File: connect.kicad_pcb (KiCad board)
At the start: 4 copper layers, 80 x 34.5 mm, 81 parts, among them J101 Cortex, J102 DX07S016JA3, J201 NE8FAH, J301 SJ2-25404B-SMT-TR, J401 SJ2-25404B-SMT-TR, SW101 SKSG, SW102 SKSG, SW103 SKSG, SW104 SKSG, SW105 SKSG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

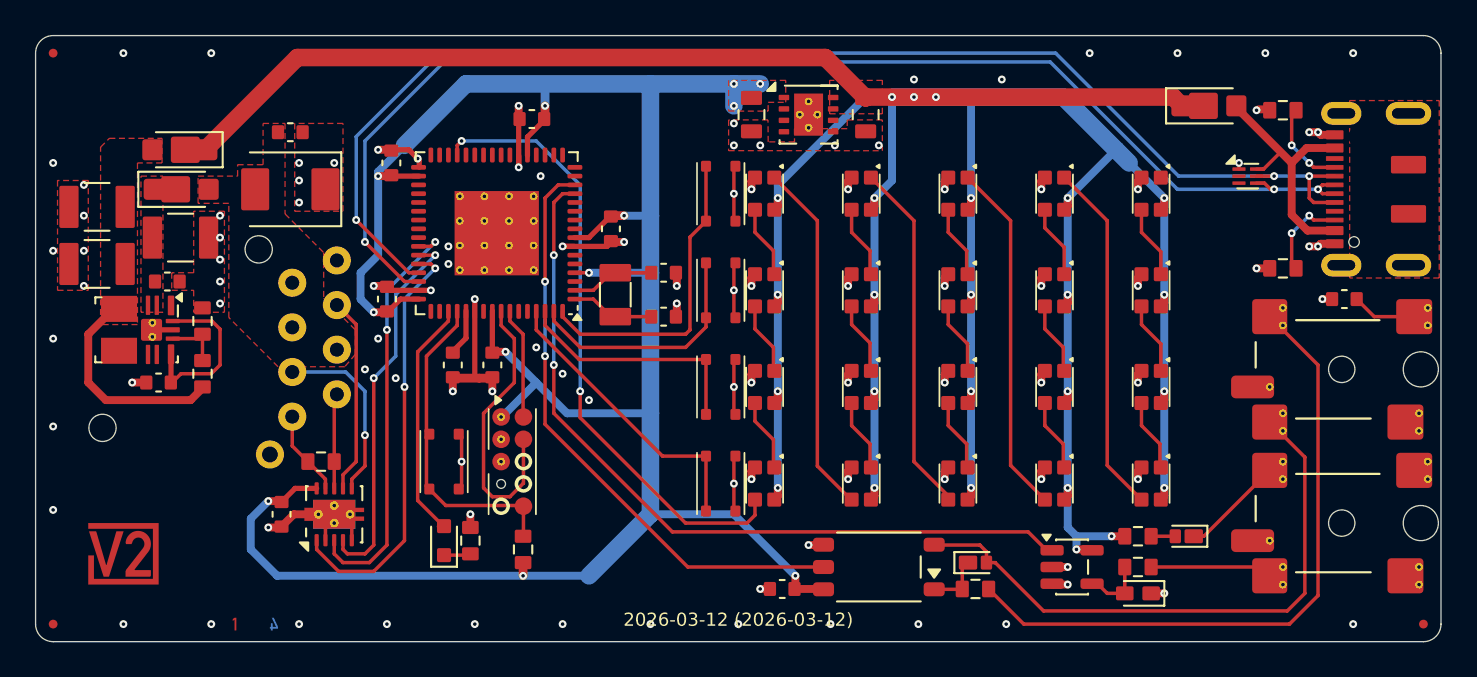
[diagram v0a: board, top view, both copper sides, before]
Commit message: Update ESD suppressor
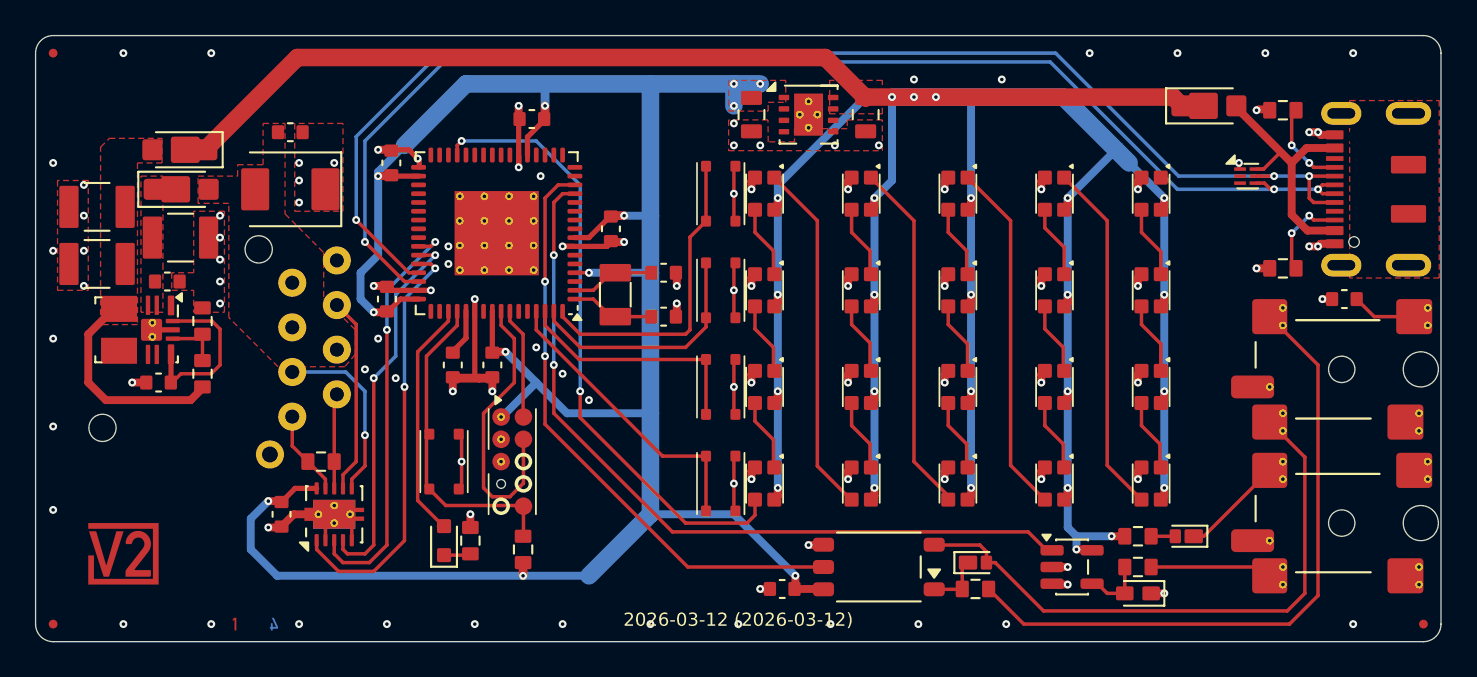
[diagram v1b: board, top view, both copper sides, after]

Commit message: Update
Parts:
- moved ESD101 2.00 mm to (133.5, 91.0)
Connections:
- ESD101 pad 2: unconnected-(ESD101-D2-Pad2) -> /USB-
- ESD101 pad 3: unconnected-(ESD101-D1-Pad3) -> /USB+
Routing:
- net +VBUS: track 14.9 -> 18.4 mm
- net /USB+: track 72.1 -> 71.6 mm, vias 3 -> 2
- net /USB-: track 73.9 -> 73.6 mm, vias 3 -> 2
- net GND: vias 106 -> 108

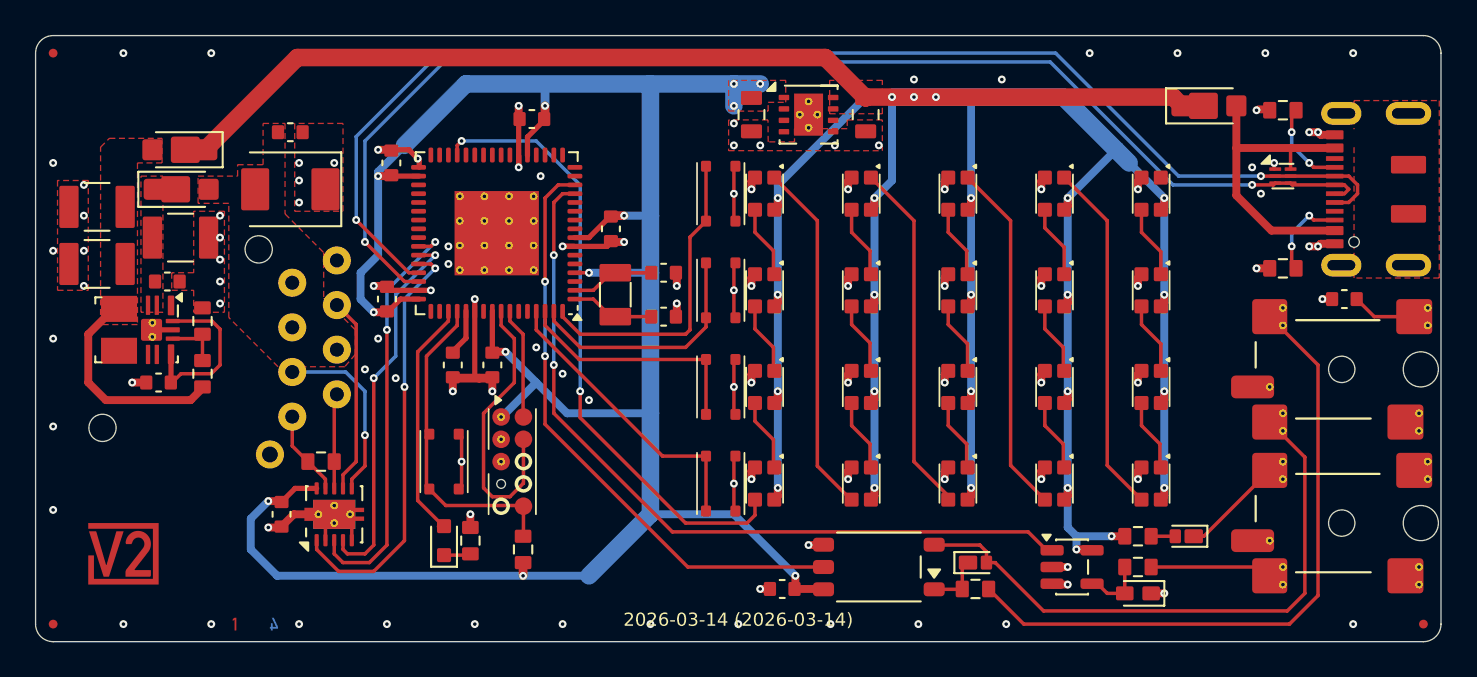
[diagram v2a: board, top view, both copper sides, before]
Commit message: KiCad 10
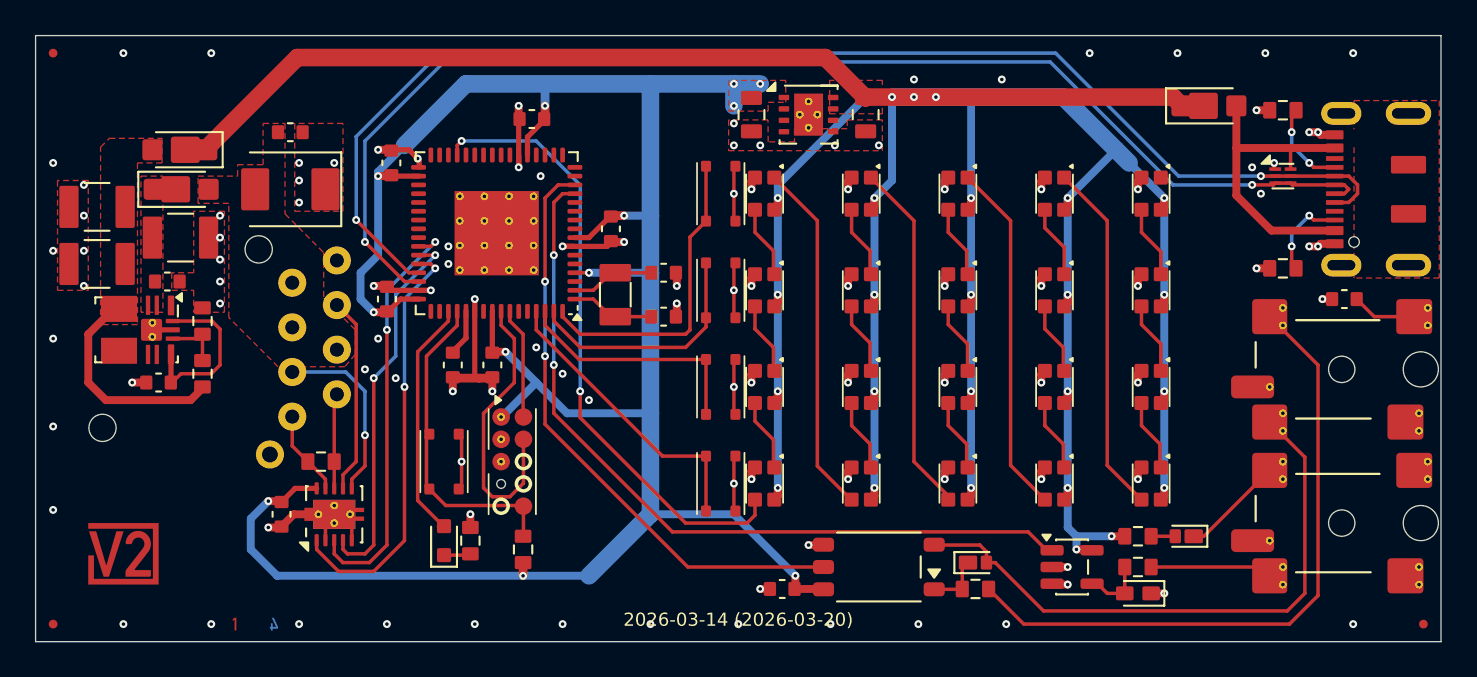
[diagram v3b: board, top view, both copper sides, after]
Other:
- outline, holes or cut-outs redrawn

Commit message: Refresh
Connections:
- net +VBUS renamed /+VBUS
- net +VLINK renamed /+VLINK
- net Shield renamed /Shield

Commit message: Refresh
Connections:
- net /VDDCORE renamed /+VDDCORE
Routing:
- net +5V: track 206.8 -> 205.3 mm
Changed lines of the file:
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@@
 	(paper "A4")
 	(title_block
-		(date "2026-03-20")
+		(date "2026-03-26")
 		(rev "2026-03-14")
 	)
@@
 			(layers "F.Cu" "F.Mask")
 			(roundrect_rratio 0.3)
-			(net "/VDDCORE")
+			(net "/+VDDCORE")
 			(pinfunction "VDDCORE_53")
 			(pintype "power_out")
@@
 			(layers "F.Cu" "F.Mask")
 			(roundrect_rratio 0.1428571429)
-			(net "/VDDCORE")
+			(net "/+VDDCORE")
 			(pintype "passive")
 		)
@@
 	)
 	(segment
+		(start 110.2 87)
+		(end 127.75 87)
+		(width 1)
+		(layer "F.Cu")
+		(net "+5V")
+	)
+	(segment
 		(start 104.75 103.25)
 		(end 104.75 103.715)
@@
 	)
 	(segment
-		(start 109.8 86.5)
-		(end 127.25 86.5)
-		(width 1)
+		(start 104.75 103.715)
+		(end 104.55 103.915)
+		(width 0.45)
 		(layer "F.Cu")
 		(net "+5V")
 	)
 	(segment
-		(start 104.75 103.715)
-		(end 104.55 103.915)
-		(width 0.45)
+		(start 109.75 86.55)
+		(end 110.2 87)
+		(width 1)
 		(layer "F.Cu")
 		(net "+5V")
@@
 	)
 	(segment
-		(start 109.75 86.55)
-		(end 109.8 86.5)
-		(width 1)
-		(layer "F.Cu")
-		(net "+5V")
-	)
-	(segment
 		(start 104.75 109.215)
 		(end 104.55 109.415)
@@
 	)
 	(segment
-		(start 127.25 86.5)
-		(end 127.75 87)
-		(width 1)
-		(layer "F.Cu")
-		(net "+5V")
-	)
-	(segment
 		(start 121.25 92.715)
 		(end 121.05 92.915)
@@
 	)
 	(via
-		(at 113.75 86.5)
+		(at 113.75 87)
 		(size 0.45)
 		(drill 0.2)
@@
 	)
 	(via
-		(at 112.5 86.5)
+		(at 112.5 87)
 		(size 0.45)
 		(drill 0.2)
@@
 	)
 	(via
-		(at 111.25 86.5)
+		(at 111.25 87)
 		(size 0.45)
 		(drill 0.2)
@@
 	)
 	(segment
+		(start 121.5 87)
+		(end 124 89.5)
+		(width 1)
+		(layer "B.Cu")
+		(net "+5V")
+	)
+	(segment
 		(start 104.75 92.25)
 		(end 104.75 97.75)
@@
 	)
 	(segment
-		(start 104.75 92.25)
-		(end 104.75 91.5)
-		(width 0.45)
-		(layer "B.Cu")
-		(net "+5V")
-	)
-	(segment
-		(start 121 86.5)
-		(end 124 89.5)
+		(start 115.75 87)
+		(end 121.5 87)
 		(width 1)
 		(layer "B.Cu")
@@
 	)
 	(segment
-		(start 115.75 86.5)
-		(end 121 86.5)
-		(width 1)
+		(start 109.25 87)
+		(end 104.75 91.5)
+		(width 0.45)
 		(layer "B.Cu")
 		(net "+5V")
@@
 	)
 	(segment
-		(start 111.25 91.25)
-		(end 111.25 86.5)
-		(width 0.45)
-		(layer "B.Cu")
-		(net "+5V")
-	)
-	(segment
 		(start 115.75 97.75)
 		(end 115.75 103.25)
@@
 	)
 	(segment
-		(start 104.75 91.5)
-		(end 109.75 86.5)
+		(start 115.75 92.25)
+		(end 115.75 87)
 		(width 0.45)
 		(layer "B.Cu")
@@
 	)
 	(segment
-		(start 115.75 92.25)
-		(end 115.75 86.5)
+		(start 121.75 112.25)
+		(end 121.75 111.5)
 		(width 0.45)
 		(layer "B.Cu")
@@
 	)
 	(segment
-		(start 109.75 86.5)
-		(end 111.25 86.5)
+		(start 104.75 103.25)
+		(end 104.75 108.75)
 		(width 0.45)
 		(layer "B.Cu")
@@
 	)
 	(segment
-		(start 121.75 112.25)
-		(end 121.75 111.5)
+		(start 111.25 91.25)
+		(end 110.25 92.25)
 		(width 0.45)
 		(layer "B.Cu")
@@
 	)
 	(segment
-		(start 104.75 103.25)
-		(end 104.75 108.75)
+		(start 121.25 92.25)
+		(end 124 89.5)
 		(width 0.45)
 		(layer "B.Cu")
@@
 	)
 	(segment
-		(start 121.25 92.25)
-		(end 124 89.5)
-		(width 0.45)
+		(start 115.75 87)
+		(end 111.25 87)
+		(width 1)
 		(layer "B.Cu")
 		(net "+5V")
@@
 	)
 	(segment
-		(start 113 86.5)
-		(end 115.75 86.5)
-		(width 1)
-		(layer "B.Cu")
-		(net "+5V")
-	)
-	(segment
 		(start 115.75 103.25)
 		(end 115.75 108.75)
@@
 	)
 	(segment
-		(start 111.25 86.5)
-		(end 113 86.5)
-		(width 1)
+		(start 111.25 87)
+		(end 109.25 87)
+		(width 0.45)
 		(layer "B.Cu")
 		(net "+5V")
@@
 	)
 	(segment
+		(start 104.75 91.5)
+		(end 104.75 92.25)
+		(width 0.45)
+		(layer "B.Cu")
+		(net "+5V")
+	)
+	(segment
 		(start 126.75 97.75)
 		(end 126.75 103.25)
@@
 	)
 	(segment
-		(start 110.25 92.25)
+		(start 111.25 87)
 		(end 111.25 91.25)
 		(width 0.45)
@@
 	)
 	(segment
-		(start 87 98.6625)
-		(end 87 100.225)
-		(width 0.3)
-		(layer "F.Cu")
-		(net "/VDDCORE")
-	)
-	(segment
-		(start 87 100.225)
-		(end 86.25 100.975)
-		(width 0.3)
-		(layer "F.Cu")
-		(net "/VDDCORE")
-	)
-	(segment
 		(start 89.75 100.25)
 		(end 89 99.5)
@@
 		(net "Net-(D101-K)")
 	)
+	(segment
+		(start 87 98.6625)
+		(end 87 100.225)
+		(width 0.3)
+		(layer "F.Cu")
+		(net "/+VDDCORE")
+	)
+	(segment
+		(start 87 100.225)
+		(end 86.25 100.975)
+		(width 0.3)
+		(layer "F.Cu")
+		(net "/+VDDCORE")
+	)
 	(zone
